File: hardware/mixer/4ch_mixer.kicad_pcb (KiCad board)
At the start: 2 copper layers, 100.8 x 45.5 mm, 40 parts, among them J1 Mic1, J1-Mic1 Conn_01x02_Pin, J1-pwr1 PWR, J2 Mic2, J2-Mic2 Conn_01x02_Pin, J3 Guitar, J3-Guitar1 Conn_01x02_Pin, J4 Line In, J4-Line-In1 Conn_01x02_Pin, J5 Line Out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

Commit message: nearly finished mixer & phones
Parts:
- removed J1: Mic1, Connector_PinHeader_2.54mm:PinHeader_1x02_P2.54mm_Vertical
- removed J2: Mic2, Connector_PinHeader_2.54mm:PinHeader_1x02_P2.54mm_Vertical
- removed J3: Guitar, Connector_PinHeader_2.54mm:PinHeader_1x02_P2.54mm_Vertical
- removed J4: Line In, Connector_PinHeader_2.54mm:PinHeader_1x02_P2.54mm_Vertical
- removed J5: Line Out, Connector_PinHeader_2.54mm:PinHeader_1x02_P2.54mm_Vertical
- removed J6: Headphones, Connector_PinHeader_2.54mm:PinHeader_1x03_P2.54mm_Vertical
- C4: footprint Capacitor_THT:C_Disc_D3.0mm_W1.6mm_P2.50mm -> Capacitor_THT:C_Disc_D10.0mm_W2.5mm_P5.00mm
- moved R13 127.0 mm to (141.5, 53.0), turned to -90 degrees
- moved J5-Out1 126.0 mm to (121.0, 53.5)
- moved R11 125.7 mm to (167.0, 56.5)
- moved J1-pwr1 120.8 mm to (164.5, 43.0), turned to -90 degrees
- moved R12 117.8 mm to (145.5, 58.0), turned to 90 degrees
- moved R8 110.5 mm to (173.0, 70.5), turned to 180 degrees
- moved R10 104.3 mm to (147.5, 65.0), turned to -90 degrees
- moved J6-phones1 103.0 mm to (167.9, 63.0)
- moved C4 101.9 mm to (167.0, 52.5)
- moved R7 95.2 mm to (120.5, 50.0), turned to 180 degrees
- moved R6 94.0 mm to (112.5, 45.0), turned to -90 degrees
- moved R9 93.7 mm to (142.0, 70.0), turned to 180 degrees
- moved R5 88.4 mm to (103.4, 45.0)
- moved RV5 73.2 mm to (115.0, 72.0)
- moved C2 72.4 mm to (107.2, 71.0), turned to 180 degrees
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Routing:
- net GND: track 78.7 -> 287.3 mm, vias 0 -> 4
- net -12V: track 0.00 -> 167.9 mm
- net +12V: track 0.00 -> 152.6 mm, vias 0 -> 2
- net Net-(U2A--): track 0.00 -> 70.6 mm, vias 0 -> 2
- net Net-(J6-phones1-Pin_1): track 0.00 -> 56.3 mm, vias 0 -> 3
- net Net-(U3B-+): track 0.00 -> 45.5 mm
- net Net-(U3A-+): track 0.00 -> 42.6 mm
- net Net-(R6-Pad2): track 0.00 -> 33.4 mm, vias 0 -> 2
- net Net-(U1B--): track 0.00 -> 29.1 mm
- net Net-(U1A--): track 28.6 -> 53.8 mm
- net Net-(R10-Pad1): track 0.00 -> 14.5 mm
- net Net-(J6-phones1-Pin_3): track 0.00 -> 14.4 mm
- net Net-(C5-Pad1): track 0.00 -> 9.22 mm
- net Net-(R4-Pad2): track 6.83 -> 13.5 mm
- net Net-(J4-Line-In1-Pin_1): track 0.00 -> 6.33 mm
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
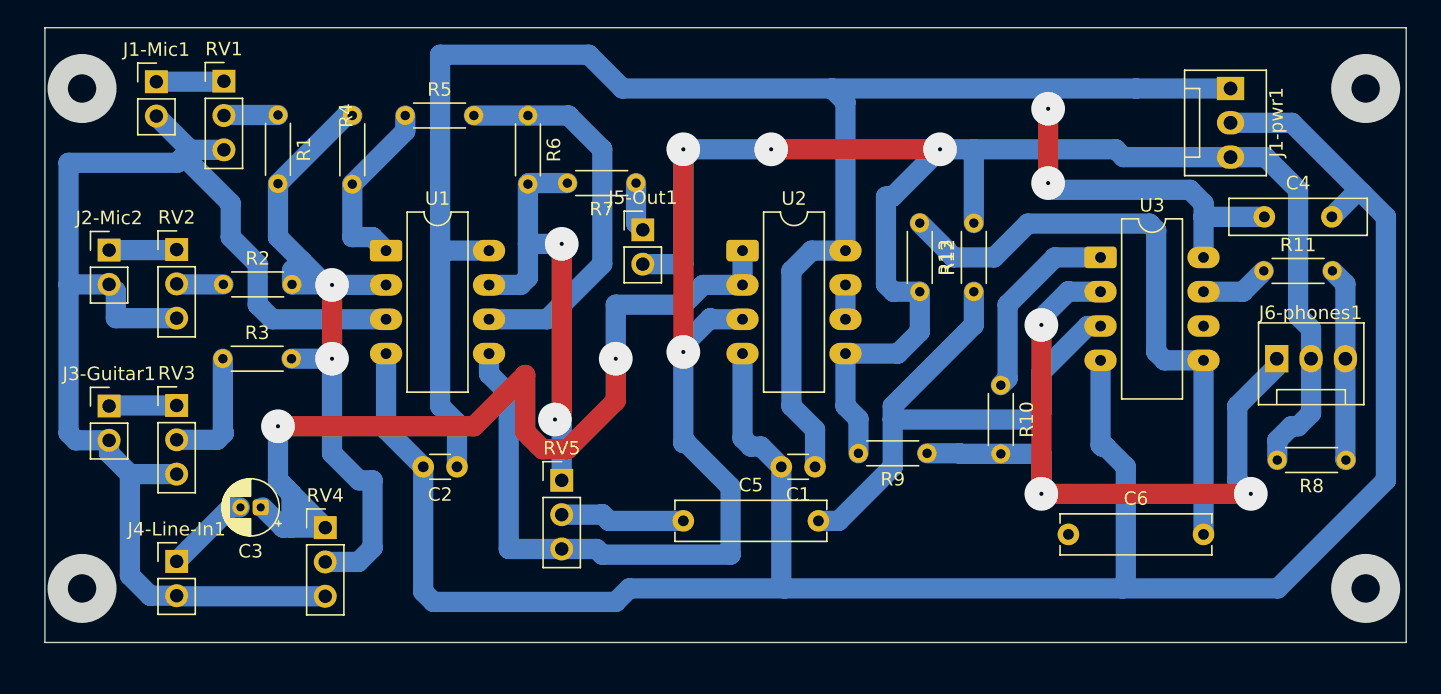
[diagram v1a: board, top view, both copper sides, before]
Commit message: Completed PCB layout
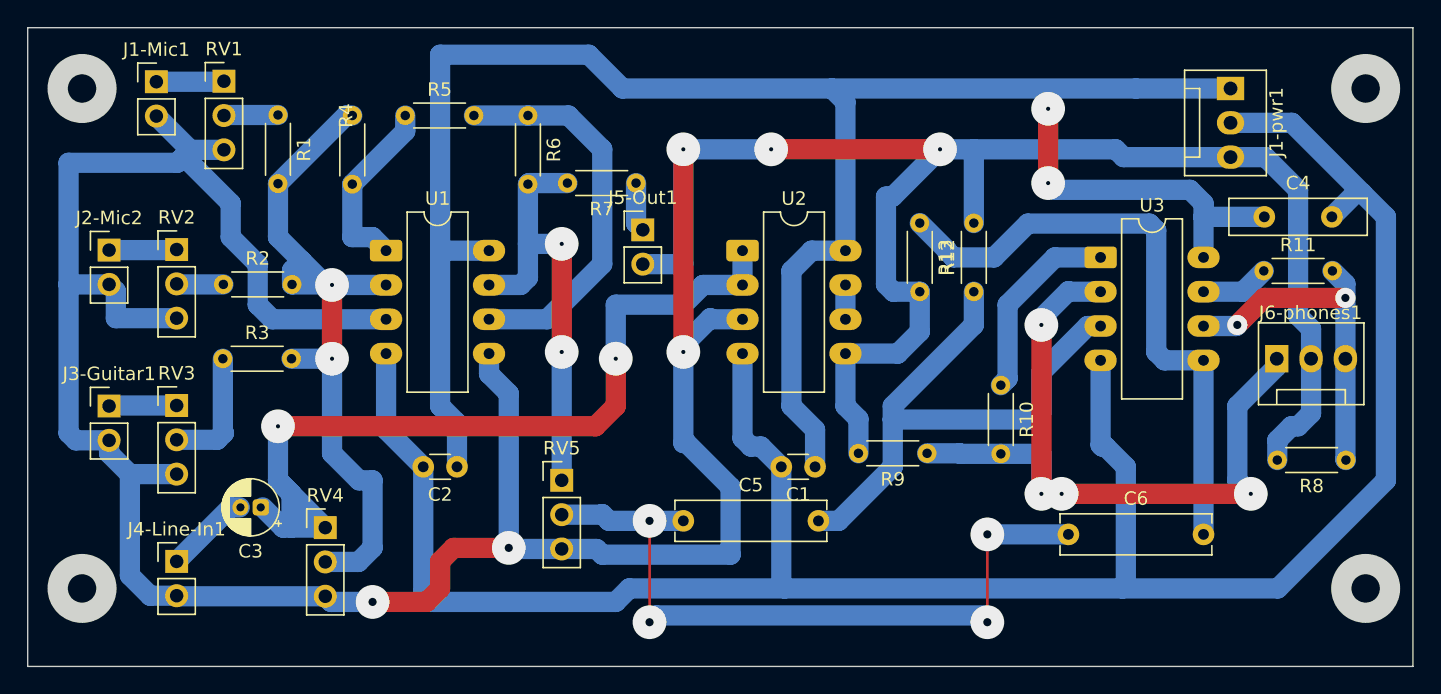
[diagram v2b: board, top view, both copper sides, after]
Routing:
- net Net-(C5-Pad1): track 9.22 -> 40.4 mm, vias 0 -> 4
- net GND: track 287.3 -> 303.8 mm, vias 4 -> 6
- net Net-(J6-phones1-Pin_3): track 14.4 -> 25.8 mm, vias 0 -> 2
- net Net-(U2A--): track 70.6 -> 63.8 mm
- net Net-(J6-phones1-Pin_1): track 56.3 -> 54.8 mm, vias 3 -> 4
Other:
- board size 100.8 x 45.5 mm -> 102.5 x 47.3 mm
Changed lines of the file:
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@@
 		)
 	)
+	(gr_line
+		(start 121.5 82.5)
+		(end 121.5 75)
+		(stroke
+			(width 0.2)
+			(type default)
+		)
+		(layer "F.Cu")
+		(net 12)
+	)
+	(gr_line
+		(start 146.5 76)
+		(end 146.5 82.5)
+		(stroke
+			(width 0.2)
+			(type default)
+		)
+		(layer "F.Cu")
+		(net 12)
+	)
 	(gr_rect
-		(start 76.75 38.5)
-		(end 177.5 84)
+		(start 75.476362 38.5)
+		(end 178 85.773638)
 		(stroke
 			(width 0.1)
@@
 	)
 	(segment
+		(start 106 80)
+		(end 105 81)
+		(width 1.5)
+		(layer "F.Cu")
+		(net 1)
+	)
+	(segment
+		(start 107 77)
+		(end 106 78)
+		(width 1.5)
+		(layer "F.Cu")
+		(net 1)
+	)
+	(segment
+		(start 105 81)
+		(end 101 81)
+		(width 1.5)
+		(layer "F.Cu")
+		(net 1)
+	)
+	(segment
+		(start 106 78)
+		(end 106 80)
+		(width 1.5)
+		(layer "F.Cu")
+		(net 1)
+	)
+	(segment
+		(start 111.08 77)
+		(end 107 77)
+		(width 1.5)
+		(layer "F.Cu")
+		(net 1)
+	)
+	(segment
 		(start 124 47.5)
 		(end 124 62.5)
@@
 	)
 	(via
+		(at 101 81)
+		(size 2.5)
+		(drill 0.6)
+		(layers "F.Cu" "B.Cu")
+		(free yes)
+		(net 1)
+	)
+	(via
+		(at 111.08 77)
+		(size 2.5)
+		(drill 0.6)
+		(layers "F.Cu" "B.Cu")
+		(free yes)
+		(net 1)
+	)
+	(via
 		(at 124 47.5)
 		(size 2.5)
@@
 	)
 	(segment
+		(start 101 81)
+		(end 97.92 81)
+		(width 1.5)
+		(layer "B.Cu")
+		(net 1)
+	)
+	(segment
 		(start 141.5 58.04)
 		(end 139.54 58.04)
@@
 	)
 	(segment
+		(start 111.08 77)
+		(end 111.08 65.58)
+		(width 1.5)
+		(layer "B.Cu")
+		(net 1)
+	)
+	(segment
 		(start 170.46 63)
 		(end 170.46 60.785)
@@
 	(segment
 		(start 111.08 77.08)
-		(end 111.08 65.58)
+		(end 111.08 77)
 		(width 1.5)
 		(layer "B.Cu")
@@
 		(start 127.5 72.5)
 		(end 127.5 77.5)
+		(width 1.5)
+		(layer "B.Cu")
+		(net 1)
+	)
+	(segment
+		(start 97.92 81)
+		(end 97.5 80.58)
 		(width 1.5)
 		(layer "B.Cu")
@@
 	)
 	(segment
-		(start 115 67)
-		(end 114.5 67.5)
-		(width 1.5)
-		(layer "F.Cu")
-		(net 7)
-	)
-	(segment
-		(start 115 54.5)
-		(end 115 67)
+		(start 115 62.5)
+		(end 115 54.5)
 		(width 1.5)
 		(layer "F.Cu")
@@
 	)
 	(via
-		(at 114.5 67.5)
+		(at 115 62.5)
 		(size 2.5)
 		(drill 0.3)
@@
 	)
 	(segment
-		(start 115 68)
-		(end 114.5 67.5)
-		(width 1.5)
-		(layer "B.Cu")
-		(net 7)
-	)
-	(segment
 		(start 115 72)
-		(end 115 68)
+		(end 115 62.5)
 		(width 1.5)
 		(layer "B.Cu")
@@
 	)
 	(segment
-		(start 112.299 64.201)
-		(end 112.299 68.411685)
+		(start 119 66.5)
+		(end 119 63)
 		(width 1.5)
 		(layer "F.Cu")
@@
 	)
 	(segment
-		(start 112.299 68.411685)
-		(end 113.588315 69.701)
+		(start 117.5 68)
+		(end 119 66.5)
 		(width 1.5)
 		(layer "F.Cu")
@@
 	(segment
 		(start 94 68)
-		(end 108.5 68)
-		(width 1.5)
-		(layer "F.Cu")
-		(net 8)
-	)
-	(segment
-		(start 119 66.112685)
-		(end 119 63)
-		(width 1.5)
-		(layer "F.Cu")
-		(net 8)
-	)
-	(segment
-		(start 108.5 68)
-		(end 112.299 64.201)
-		(width 1.5)
-		(layer "F.Cu")
-		(net 8)
-	)
-	(segment
-		(start 115.411685 69.701)
-		(end 119 66.112685)
-		(width 1.5)
-		(layer "F.Cu")
-		(net 8)
-	)
-	(segment
-		(start 113.588315 69.701)
-		(end 115.411685 69.701)
+		(end 117.5 68)
 		(width 1.5)
 		(layer "F.Cu")
@@
 		(net 11)
 	)
+	(via
+		(at 121.5 75)
+		(size 2.5)
+		(drill 0.6)
+		(layers "F.Cu" "B.Cu")
+		(net 12)
+	)
+	(via
+		(at 121.5 82.5)
+		(size 2.5)
+		(drill 0.6)
+		(layers "F.Cu" "B.Cu")
+		(free yes)
+		(net 12)
+	)
+	(via
+		(at 146.5 82.5)
+		(size 2.5)
+		(drill 0.6)
+		(layers "F.Cu" "B.Cu")
+		(free yes)
+		(net 12)
+	)
+	(via
+		(at 146.5 76)
+		(size 2.5)
+		(drill 0.6)
+		(layers "F.Cu" "B.Cu")
+		(free yes)
+		(net 12)
+	)
+	(segment
+		(start 121.5 75)
+		(end 118.5 75)
+		(width 1.5)
+		(layer "B.Cu")
+		(net 12)
+	)
 	(segment
 		(start 117.96 74.54)
@@
 	)
 	(segment
+		(start 152.5 76)
+		(end 146.5 76)
+		(width 1.5)
+		(layer "B.Cu")
+		(net 12)
+	)
+	(segment
 		(start 118.5 75)
 		(end 118 74.5)
@@
 	)
 	(segment
+		(start 122 82)
+		(end 121.5 82.5)
+		(width 1.5)
+		(layer "B.Cu")
+		(net 12)
+	)
+	(segment
+		(start 146.5 82)
+		(end 122 82)
+		(width 1.5)
+		(layer "B.Cu")
+		(net 12)
+	)
+	(segment
 		(start 124 75)
-		(end 118.5 75)
+		(end 121.5 75)
 		(width 1.5)
 		(layer "B.Cu")
@@
 	)
 	(segment
+		(start 167 58.5)
+		(end 165 60.5)
+		(width 1.5)
+		(layer "F.Cu")
+		(net 23)
+	)
+	(segment
+		(start 173 58.5)
+		(end 167 58.5)
+		(width 1.5)
+		(layer "F.Cu")
+		(net 23)
+	)
+	(via
+		(at 165 60.5)
+		(size 1.5)
+		(drill 0.6)
+		(layers "F.Cu" "B.Cu")
+		(free yes)
+		(net 23)
+	)
+	(via
+		(at 173 58.5)
+		(size 1.5)
+		(drill 0.6)
+		(layers "F.Cu" "B.Cu")
+		(free yes)
+		(net 23)
+	)
+	(segment
 		(start 173 63)
 		(end 173 70.46)
@@
 	)
 	(segment
+		(start 164.92 60.58)
+		(end 165 60.5)
+		(width 1.5)
+		(layer "B.Cu")
+		(net 23)
+	)
+	(segment
 		(start 173 57.46)
-		(end 173 63)
+		(end 173 58.5)
 		(width 1.5)
 		(layer "B.Cu")
@@
 	)
 	(segment
+		(start 173 58.5)
+		(end 173 63)
+		(width 1.5)
+		(layer "B.Cu")
+		(net 23)
+	)
+	(segment
 		(start 173 70.46)
 		(end 173.04 70.5)
@@
 	)
 	(segment
+		(start 162.5 60.58)
+		(end 164.92 60.58)
+		(width 1.5)
+		(layer "B.Cu")
+		(net 23)
+	)
+	(segment
+		(start 152 73)
+		(end 166 73)
+		(width 1.5)
+		(layer "F.Cu")
+		(net 24)
+	)
+	(segment
 		(start 150.5 60.5)
 		(end 150.5 73)
@@
 		(net 24)
 	)
-	(segment
-		(start 150.5 73)
-		(end 166 73)
-		(width 1.5)
-		(layer "F.Cu")
+	(via
+		(at 152 73)
+		(size 2.5)
+		(drill 0.3)
+		(layers "F.Cu" "B.Cu")
+		(free yes)
 		(net 24)
 	)
